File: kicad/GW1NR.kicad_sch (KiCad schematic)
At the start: 27 parts, among them U3 74ALVC164245DGG,51, U4 74ALVC164245DGG,51, U5 GW1NR-4&4B_QN881

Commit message: added title to all circuit diagrams and sub-circuit diagrams, and PDF export
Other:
- title: (none) -> GW1NR-4 FPGA and level shifter
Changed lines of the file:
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@@
 (kicad_sch (version 20211123) (generator eeschema)
   (paper "A4")
+  (title_block
+    (title "GW1NR-4 FPGA and level shifter")
+  )
   (junction (at 93.98 59.69) (diameter 0) (color 0 0 0 0)
   )

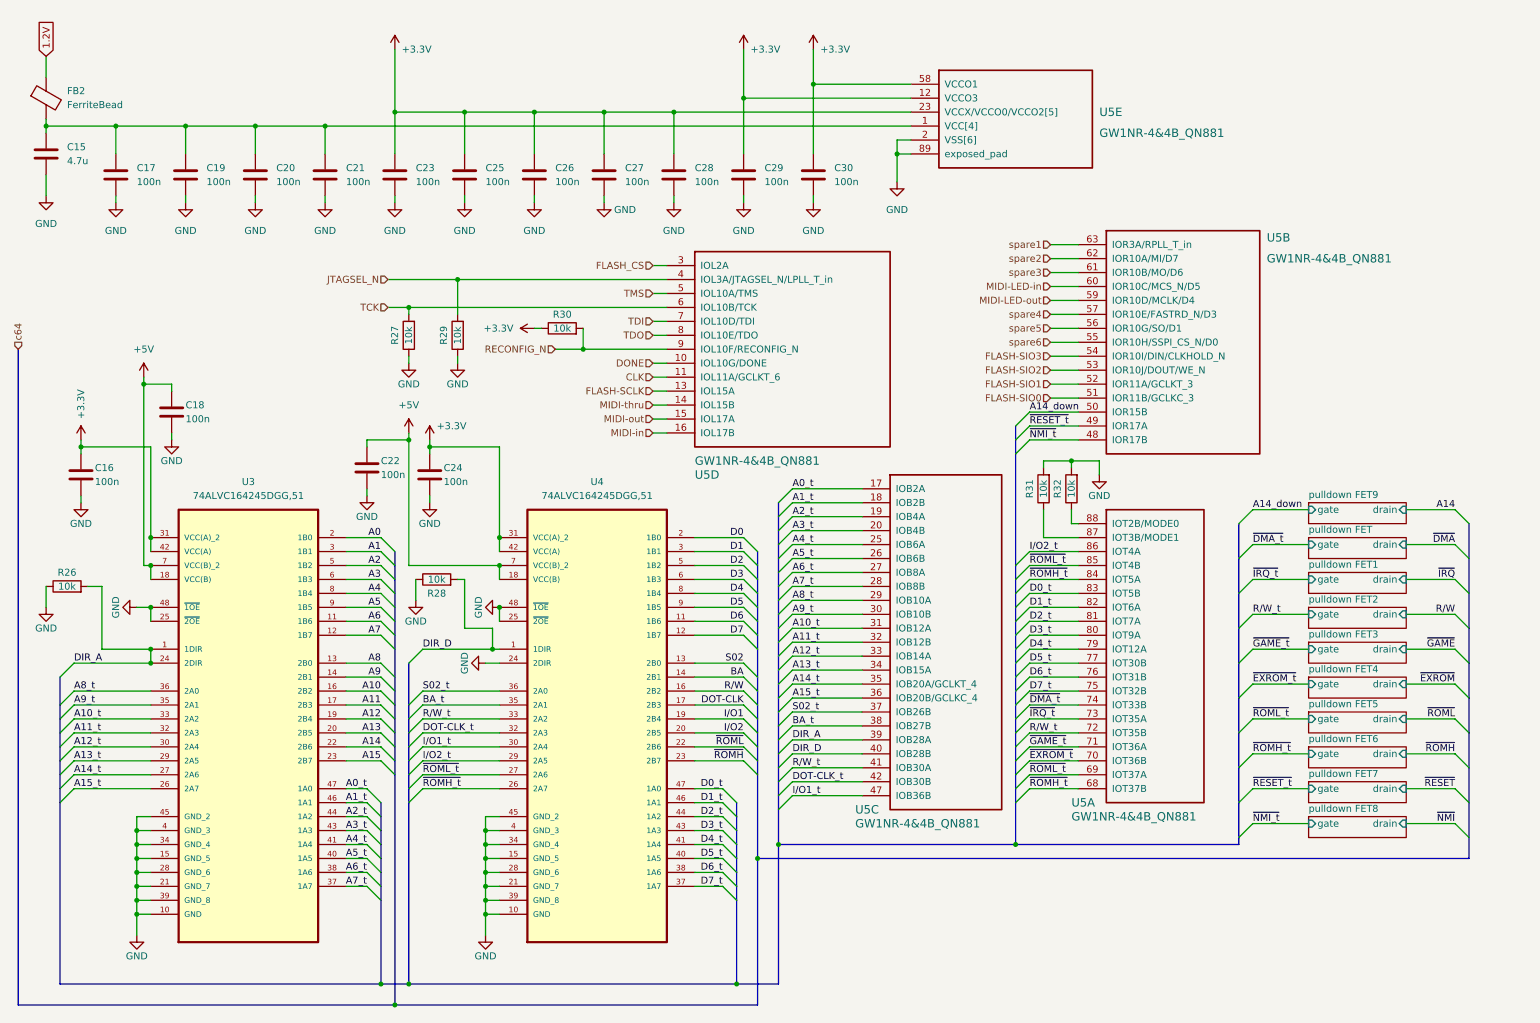
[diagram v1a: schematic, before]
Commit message: new flash, and IEC interface added
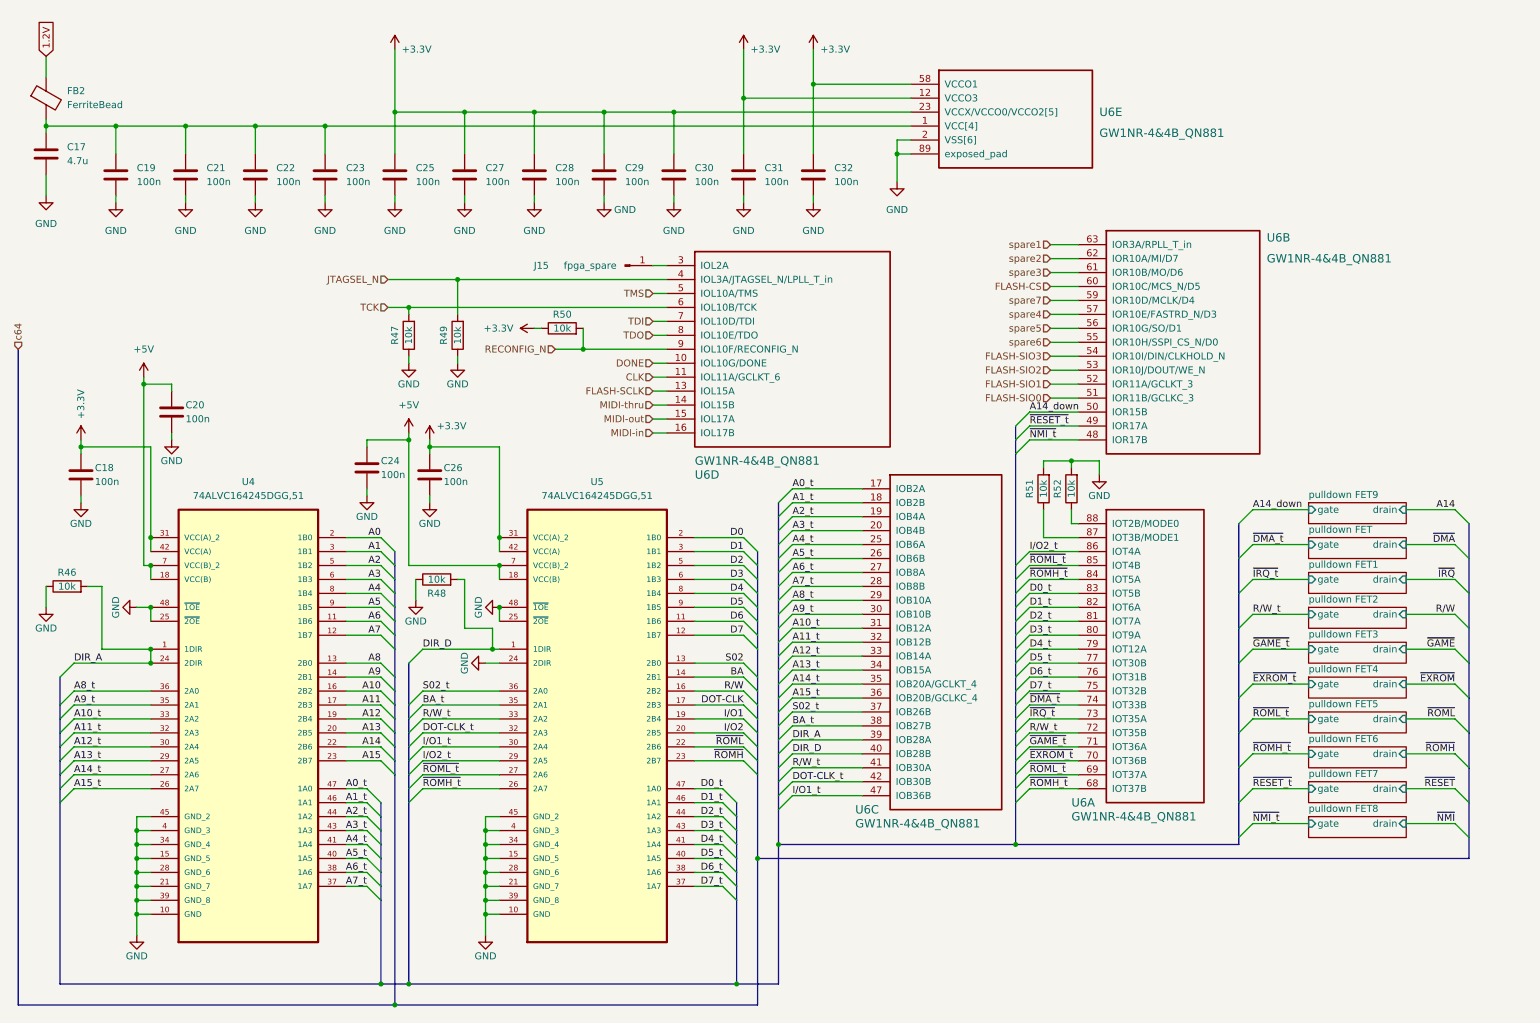
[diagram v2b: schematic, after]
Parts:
- added J15: fpga_spare, Connector_PinHeader_2.54mm:PinHeader_1x01_P2.54mm_Vertical, symbol Connector:Conn_01x01_Male
- C18: renamed from C16; footprint Capacitor_SMD:C_0402_1005Metric -> Capacitor_SMD:C_0805_2012Metric
- C19: renamed from C17; footprint Capacitor_SMD:C_0402_1005Metric -> Capacitor_SMD:C_0805_2012Metric
- C20: renamed from C18; footprint Capacitor_SMD:C_0402_1005Metric -> Capacitor_SMD:C_0805_2012Metric
- C21: renamed from C19; footprint Capacitor_SMD:C_0402_1005Metric -> Capacitor_SMD:C_0805_2012Metric
- C22: renamed from C20; footprint Capacitor_SMD:C_0402_1005Metric -> Capacitor_SMD:C_0805_2012Metric
- C23: renamed from C21; footprint Capacitor_SMD:C_0402_1005Metric -> Capacitor_SMD:C_0805_2012Metric
- C24: renamed from C22; footprint Capacitor_SMD:C_0402_1005Metric -> Capacitor_SMD:C_0805_2012Metric
- C25: renamed from C23; footprint Capacitor_SMD:C_0402_1005Metric -> Capacitor_SMD:C_0805_2012Metric
- C26: renamed from C24; footprint Capacitor_SMD:C_0402_1005Metric -> Capacitor_SMD:C_0805_2012Metric
- C27: renamed from C25; footprint Capacitor_SMD:C_0402_1005Metric -> Capacitor_SMD:C_0805_2012Metric
- C28: renamed from C26; footprint Capacitor_SMD:C_0402_1005Metric -> Capacitor_SMD:C_0805_2012Metric
- C29: renamed from C27; footprint Capacitor_SMD:C_0402_1005Metric -> Capacitor_SMD:C_0805_2012Metric
- C30: renamed from C28; footprint Capacitor_SMD:C_0402_1005Metric -> Capacitor_SMD:C_0805_2012Metric
- C31: renamed from C29; footprint Capacitor_SMD:C_0402_1005Metric -> Capacitor_SMD:C_0805_2012Metric
- C32: renamed from C30; footprint Capacitor_SMD:C_0402_1005Metric -> Capacitor_SMD:C_0805_2012Metric
- R46: renamed from R26; footprint Resistor_SMD:R_0402_1005Metric -> Resistor_SMD:R_0805_2012Metric
- R47: renamed from R27; footprint Resistor_SMD:R_0402_1005Metric -> Resistor_SMD:R_0805_2012Metric
- R48: renamed from R28; footprint Resistor_SMD:R_0402_1005Metric -> Resistor_SMD:R_0805_2012Metric
- R49: renamed from R29; footprint Resistor_SMD:R_0402_1005Metric -> Resistor_SMD:R_0805_2012Metric
- R50: renamed from R30; footprint Resistor_SMD:R_0402_1005Metric -> Resistor_SMD:R_0805_2012Metric
- R51: renamed from R31; footprint Resistor_SMD:R_0402_1005Metric -> Resistor_SMD:R_0805_2012Metric
- R52: renamed from R32; footprint Resistor_SMD:R_0402_1005Metric -> Resistor_SMD:R_0805_2012Metric
- renumbered C15 to C17, U3 to U4, U4 to U5, U5 to U6
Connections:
- net FLASH_CS: no longer names the net of U6.3 (IOL2A)
- net FLASH_CS: now also J15.1 (Pin_1)
- net MIDI-LED-in renamed FLASH-CS
- net MIDI-LED-out renamed spare7

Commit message: circuit improvements fixed the level shifter circuit, added the shield pins to the reset button, and replaced the IEC circuit with unused pins of the 16 bit level shifter, and a new 6 channel open collector driver
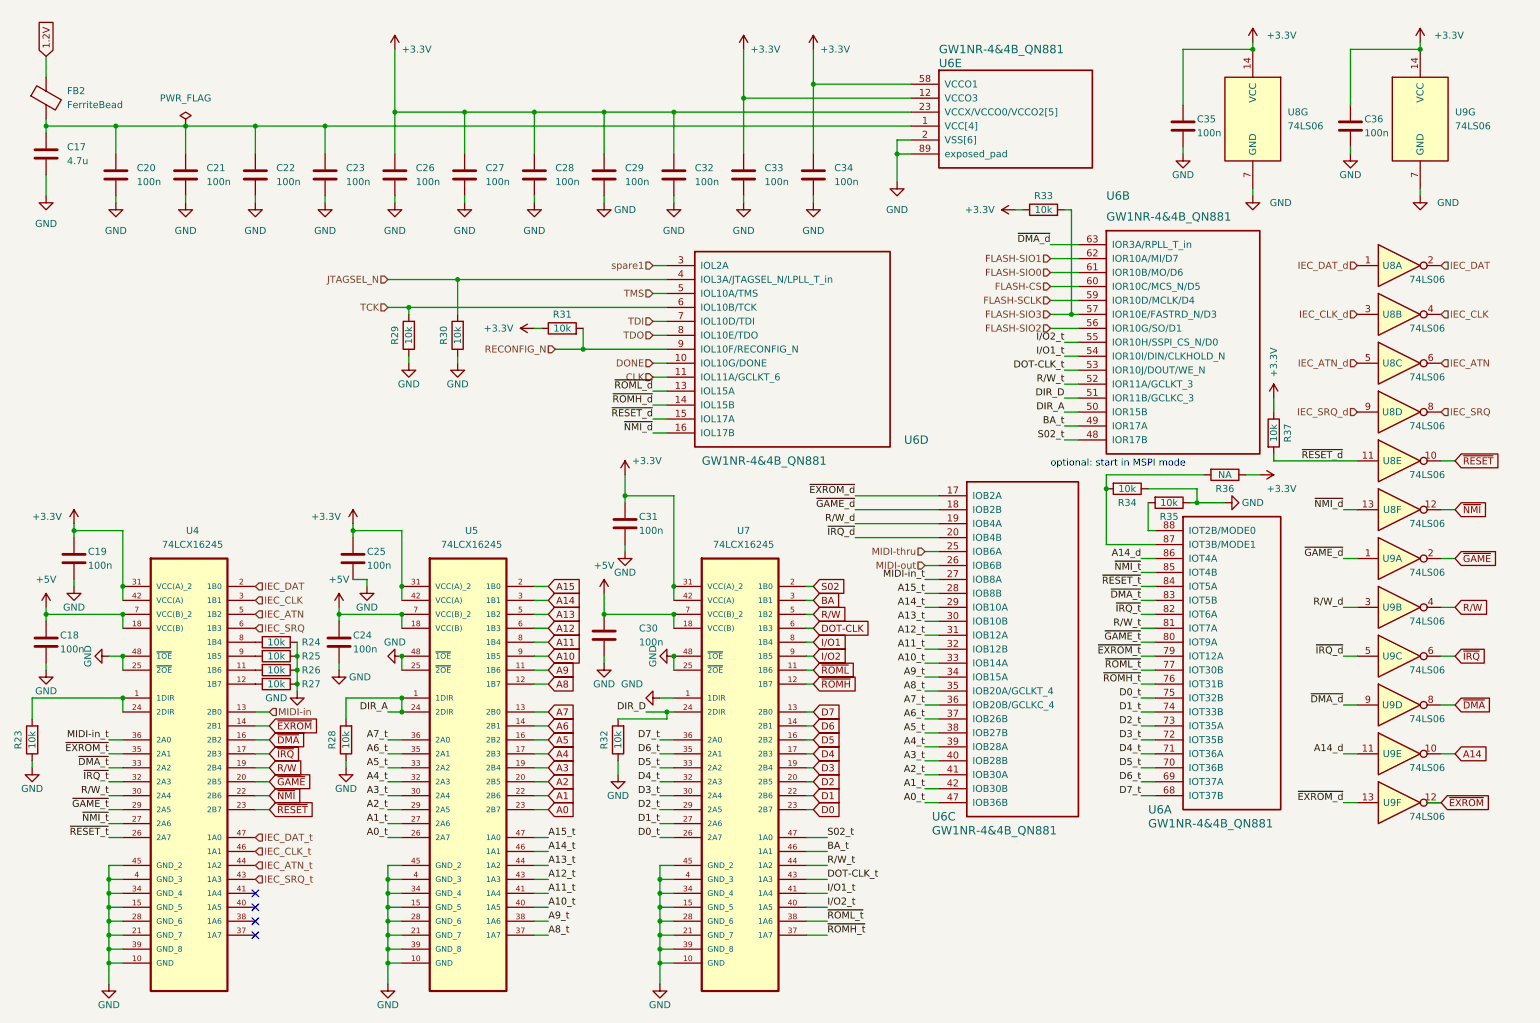
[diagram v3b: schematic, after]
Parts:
- removed J15: fpga_spare, Connector_PinHeader_2.54mm:PinHeader_1x01_P2.54mm_Vertical, symbol Connector:Conn_01x01_Male
- added C18, C19, C35, C36: 100n, Capacitor_SMD:C_0805_2012Metric, symbol Device:C
- added R23, R24, R25, R26, R27, R33, R37: 10k, Resistor_SMD:R_0805_2012Metric, symbol Device:R
- added R36: NA, Resistor_SMD:R_0805_2012Metric, symbol Device:R
- added U4: 74LCX16245, SOP50:SOP50P810X120-48N, symbol 74ALVC164245DGG_51:74ALVC164245DGG,51
- added U8, U9: 74LS06, Package_SO:SO-14_3.9x8.65mm_P1.27mm, symbol 74xx:74LS06
- U5: renamed from U4; value 74ALVC164245DGG,51 -> 74LCX16245; footprint Package_SO:TSSOP-48_8x12.5mm_P0.5mm -> SOP50:SOP50P810X120-48N
- U7: renamed from U5; value 74ALVC164245DGG,51 -> 74LCX16245; footprint Package_SO:TSSOP-48_8x12.5mm_P0.5mm -> SOP50:SOP50P810X120-48N
- renumbered C19 to C20, C20 to C24, C18 to C25, C25 to C26, C24 to C30, C26 to C31, C30 to C32, C31 to C33, C32 to C34, R46 to R28, R47 to R29, R49 to R30, R50 to R31, R48 to R32, R51 to R34, R52 to R35
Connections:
- net A14_down is gone; now on net DIR_A: U6.50 (IOR15B)
- net spare2 is gone; now on net FLASH-SIO1: U6.62 (IOR10A/MI/D7)
- net spare3 is gone; now on net FLASH-SIO0: U6.61 (IOR10B/MO/D6)
- net spare4 is gone; now on net FLASH-SIO3: U6.57 (IOR10E/FASTRD_N/D3)
- net spare5 is gone; now on net FLASH-SIO2: U6.56 (IOR10G/SO/D1)
- net spare6 is gone; now on net I/O2_t: U6.55 (IOR10H/SSPI_CS_N/D0)
- net spare7 is gone; now on net FLASH-SCLK: U6.59 (IOR10D/MCLK/D4)
- net +3.3V: now also C19.1, C35.1, C36.1, R33.1, R36.1, R37.1, U4.31 (VCC(A)_2), U4.42 (VCC(A)), U8.14 (VCC), U9.14 (VCC)
- net +5V: now also C18.1, U4.18 (VCC(B)), U4.7 (VCC(B)_2)
- net A0: now also U5.23 (2B7); no longer U5.2 (1B0)
- net A0_t: now also U5.26 (2A7), U6.47 (IOB36B); no longer U5.47 (1A0), U6.17 (IOB2A)
- net A1: now also U5.22 (2B6); no longer U5.3 (1B1)
- net A10: now also U5.9 (1B5); no longer U5.16 (2B2)
- net A10_t: now also U5.40 (1A5), U6.33 (IOB14A); no longer U5.33 (2A2), U6.31 (IOB12A)
- net A11: now also U5.8 (1B4); no longer U5.17 (2B3)
- net A11_t: now also U5.41 (1A4); no longer U5.32 (2A3)
- net A12: now also U5.6 (1B3); no longer U5.19 (2B4)
- net A12_t: now also U5.43 (1A3), U6.31 (IOB12A); no longer U5.30 (2A4), U6.33 (IOB14A)
- net A13: now also U5.5 (1B2); no longer U5.20 (2B5)
- net A13_t: now also U5.44 (1A2), U6.30 (IOB10B); no longer U5.29 (2A5), U6.34 (IOB15A)
- net A14: now also U5.3 (1B1), U9.10; no longer U5.22 (2B6)
- net A14_t: now also U5.46 (1A1), U6.29 (IOB10A); no longer U5.27 (2A6), U6.35 (IOB20A/GCLKT_4)
- net A15: now also U5.2 (1B0); no longer U5.23 (2B7)
- net A15_t: now also U5.47 (1A0), U6.28 (IOB8B); no longer U5.26 (2A7), U6.36 (IOB20B/GCLKC_4)
- net A1_t: now also U5.27 (2A6), U6.42 (IOB30B); no longer U5.46 (1A1), U6.18 (IOB2B)
- net A2: now also U5.20 (2B5); no longer U5.5 (1B2)
- net A2_t: now also U5.29 (2A5), U6.41 (IOB30A); no longer U5.44 (1A2), U6.19 (IOB4A)
- net A3: now also U5.19 (2B4); no longer U5.6 (1B3)
- net A3_t: now also U5.30 (2A4), U6.40 (IOB28B); no longer U5.43 (1A3), U6.20 (IOB4B)
- net A4: now also U5.17 (2B3); no longer U5.8 (1B4)
- net A4_t: now also U5.32 (2A3), U6.39 (IOB28A); no longer U5.41 (1A4), U6.25 (IOB6A)
- net A5: now also U5.16 (2B2); no longer U5.9 (1B5)
- net A5_t: now also U5.33 (2A2), U6.38 (IOB27B); no longer U5.40 (1A5), U6.26 (IOB6B)
- net A6: now also U5.14 (2B1); no longer U5.11 (1B6)
- net A6_t: now also U5.35 (2A1), U6.37 (IOB26B); no longer U5.38 (1A6), U6.27 (IOB8A)
- net A7: now also U5.13 (2B0); no longer U5.12 (1B7)
- net A7_t: now also U5.36 (2A0), U6.36 (IOB20B/GCLKC_4); no longer U5.37 (1A7), U6.28 (IOB8B)
- net A8: now also U5.12 (1B7); no longer U5.13 (2B0)
- net A8_t: now also U5.37 (1A7), U6.35 (IOB20A/GCLKT_4); no longer U5.36 (2A0), U6.29 (IOB10A)
- net A9: now also U5.11 (1B6); no longer U5.14 (2B1)
- net A9_t: now also U5.38 (1A6), U6.34 (IOB15A); no longer U5.35 (2A1), U6.30 (IOB10B)
- net BA: now also U7.3 (1B1); no longer U7.14 (2B1)
- net BA_t: now also U6.49 (IOR17A), U7.46 (1A1); no longer U6.38 (IOB27B), U7.35 (2A1)
- net D0: now also U7.23 (2B7); no longer U7.2 (1B0)
- net D0_t: now also U6.75 (IOT32B), U7.26 (2A7); no longer U6.83 (IOT5B), U7.47 (1A0)
- net D1: now also U7.22 (2B6); no longer U7.3 (1B1)
- net D1_t: now also U6.74 (IOT33B), U7.27 (2A6); no longer U6.82 (IOT6A), U7.46 (1A1)
- net D2: now also U7.20 (2B5); no longer U7.5 (1B2)
- net D2_t: now also U6.73 (IOT35A), U7.29 (2A5); no longer U6.81 (IOT7A), U7.44 (1A2)
- net D3: now also U7.19 (2B4); no longer U7.6 (1B3)
- net D3_t: now also U6.72 (IOT35B), U7.30 (2A4); no longer U6.80 (IOT9A), U7.43 (1A3)
- net D4: now also U7.17 (2B3); no longer U7.8 (1B4)
- net D4_t: now also U6.71 (IOT36A), U7.32 (2A3); no longer U6.79 (IOT12A), U7.41 (1A4)
- net D5: now also U7.16 (2B2); no longer U7.9 (1B5)
- net D5_t: now also U6.70 (IOT36B), U7.33 (2A2); no longer U6.77 (IOT30B), U7.40 (1A5)
- net D6: now also U7.14 (2B1); no longer U7.11 (1B6)
- net D6_t: now also U6.69 (IOT37A), U7.35 (2A1); no longer U6.76 (IOT31B), U7.38 (1A6)
- net D7: now also U7.13 (2B0); no longer U7.12 (1B7)
- net D7_t: now also U6.68 (IOT37B), U7.36 (2A0); no longer U6.75 (IOT32B), U7.37 (1A7)
- net DIR_A: no longer U6.39 (IOB28A)
- net DIR_D: now also U6.51 (IOR11B/GCLKC_3), U7.24 (2DIR); no longer U6.40 (IOB28B), U7.1 (1DIR)
- net DOT-CLK: now also U7.6 (1B3); no longer U7.17 (2B3)
- net DOT-CLK_t: now also U6.53 (IOR10J/DOUT/WE_N), U7.43 (1A3); no longer U6.42 (IOB30B), U7.32 (2A3)
- net FLASH-SCLK: no longer U6.13 (IOL15A)
- net FLASH-SIO0: no longer U6.51 (IOR11B/GCLKC_3)
- net FLASH-SIO1: no longer U6.52 (IOR11A/GCLKT_3)
- net FLASH-SIO2: no longer U6.53 (IOR10J/DOUT/WE_N)
- net FLASH-SIO3: now also R33.2; no longer U6.54 (IOR10I/DIN/CLKHOLD_N)
- net GND: now also R34.1, R35.1, U7.1 (1DIR), C18.2, C19.2, C35.2, C36.2, R23.1, R24.1, R25.1, R26.1, R27.1, U4.10 (GND), U4.15 (GND_5), U4.21 (GND_7), U4.25 (~{2OE}), U4.28 (GND_6), U4.34 (GND_4), U4.39 (GND_8), U4.4 (GND_3), U4.45 (GND_2), U4.48 (~{1OE}), U8.7 (GND), U9.7 (GND); no longer R34.2, R35.2, U7.24 (2DIR)
- net I/O1: now also U7.8 (1B4); no longer U7.19 (2B4)
- net I/O1_t: now also U6.54 (IOR10I/DIN/CLKHOLD_N), U7.41 (1A4); no longer U6.47 (IOB36B), U7.30 (2A4)
- net I/O2: now also U7.9 (1B5); no longer U7.20 (2B5)
- net I/O2_t: now also U7.40 (1A5); no longer U6.86 (IOT4A), U7.29 (2A5)
- net MIDI-in: now also U4.13 (2B0); no longer U6.16 (IOL17B)
- net MIDI-out: now also U6.26 (IOB6B); no longer U6.15 (IOL17A)
- net MIDI-thru: now also U6.25 (IOB6A); no longer U6.14 (IOL15B)
- net R/W: now also U7.5 (1B2), U4.19 (2B4), U9.4; no longer U7.16 (2B2)
- net R/W_t: now also U6.52 (IOR11A/GCLKT_3), U6.81 (IOT7A), U7.44 (1A2), U4.30 (2A4); no longer U6.41 (IOB30A), U6.72 (IOT35B), U7.33 (2A2)
- net S02: now also U7.2 (1B0); no longer U7.13 (2B0)
- net S02_t: now also U6.48 (IOR17B), U7.47 (1A0); no longer U6.37 (IOB26B), U7.36 (2A0)
- net spare1: now also U6.3 (IOL2A); no longer U6.63 (IOR3A/RPLL_T_in)
- net ~{DMA_t}: now also U6.83 (IOT5B), U4.33 (2A2); no longer U6.74 (IOT33B)
- net ~{DMA}: now also U4.16 (2B2), U9.8
- net ~{EXROM_t}: now also U6.79 (IOT12A), U4.35 (2A1); no longer U6.70 (IOT36B)
- net ~{EXROM}: now also U4.14 (2B1), U9.12
- net ~{GAME_t}: now also U6.80 (IOT9A), U4.29 (2A5); no longer U6.71 (IOT36A)
- net ~{GAME}: now also U4.20 (2B5), U9.2
- net ~{IRQ_t}: now also U6.82 (IOT6A), U4.32 (2A3); no longer U6.73 (IOT35A)
- net ~{IRQ}: now also U4.17 (2B3), U9.6
- net ~{NMI_t}: now also U6.85 (IOT4B), U4.27 (2A6); no longer U6.48 (IOR17B)
- net ~{NMI}: now also U4.22 (2B6), U8.12
- net ~{RESET_t}: now also U6.84 (IOT5A), U4.26 (2A7); no longer U6.49 (IOR17A)
- net ~{RESET}: now also U4.23 (2B7), U8.10
- net ~{ROMH_t}: now also U6.76 (IOT31B), U7.37 (1A7); no longer U6.68 (IOT37B), U6.84 (IOT5A), U7.26 (2A7)
- net ~{ROMH}: now also U7.12 (1B7); no longer U7.23 (2B7)
- net ~{ROML_t}: now also U6.77 (IOT30B), U7.38 (1A6); no longer U6.69 (IOT37A), U6.85 (IOT4B), U7.27 (2A6)
- net ~{ROML}: now also U7.11 (1B6); no longer U7.22 (2B6)
- net at U6.87 (IOT3B/MODE1): now also R34.2, R36.2; no longer R34.1
- net at U6.88 (IOT2B/MODE0): now also R35.2; no longer R35.1
- new net: R25.2, U4.9 (1B5)
- new net: R23.2, U4.1 (1DIR), U4.24 (2DIR)
- new net: R26.2, U4.11 (1B6)
- new net: R27.2, U4.12 (1B7)
- new net: R24.2, U4.8 (1B4)
- new net A14_d: U6.86 (IOT4A), U9.11
- new net IEC_ATN: U4.5 (1B2), U8.6
- new net IEC_ATN_d: U8.5
- new net IEC_ATN_t: U4.44 (1A2)
- new net IEC_CLK: U4.3 (1B1), U8.4
- new net IEC_CLK_d: U8.3
- new net IEC_CLK_t: U4.46 (1A1)
- new net IEC_DAT: U4.2 (1B0), U8.2
- new net IEC_DAT_d: U8.1
- new net IEC_DAT_t: U4.47 (1A0)
- new net IEC_SRQ: U4.6 (1B3), U8.8
- new net IEC_SRQ_d: U8.9
- new net IEC_SRQ_t: U4.43 (1A3)
- new net MIDI-in_t: U4.36 (2A0), U6.27 (IOB8A)
- new net R/W_d: U6.19 (IOB4A), U9.3
- new net ~{DMA_d}: U6.63 (IOR3A/RPLL_T_in), U9.9
- new net ~{EXROM_d}: U6.17 (IOB2A), U9.13
- new net ~{GAME_d}: U6.18 (IOB2B), U9.1
- new net ~{IRQ_d}: U6.20 (IOB4B), U9.5
- new net ~{NMI_d}: U6.16 (IOL17B), U8.13
- new net ~{RESET_d}: R37.2, U6.15 (IOL17A), U8.11
- new net ~{ROMH_d}: U6.14 (IOL15B)
- new net ~{ROML_d}: U6.13 (IOL15A)
- no-connect marks 0 -> 4
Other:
- removed sheet pulldown FET
- removed sheet pulldown FET1
- removed sheet pulldown FET2
- removed sheet pulldown FET3
- removed sheet pulldown FET4
- removed sheet pulldown FET5
- removed sheet pulldown FET6
- removed sheet pulldown FET7
- removed sheet pulldown FET8
- removed sheet pulldown FET9
- note added: "optional: start in MSPI mode"
- moved on the sheet: C24, C25, C30, C31, R28, R32, R34, R35, U5, U6A, U6C, U7
